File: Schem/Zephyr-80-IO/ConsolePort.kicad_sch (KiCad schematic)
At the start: 12 parts, among them J2 Conn_01x04, J3 0480370001, U2 FT230XS-U

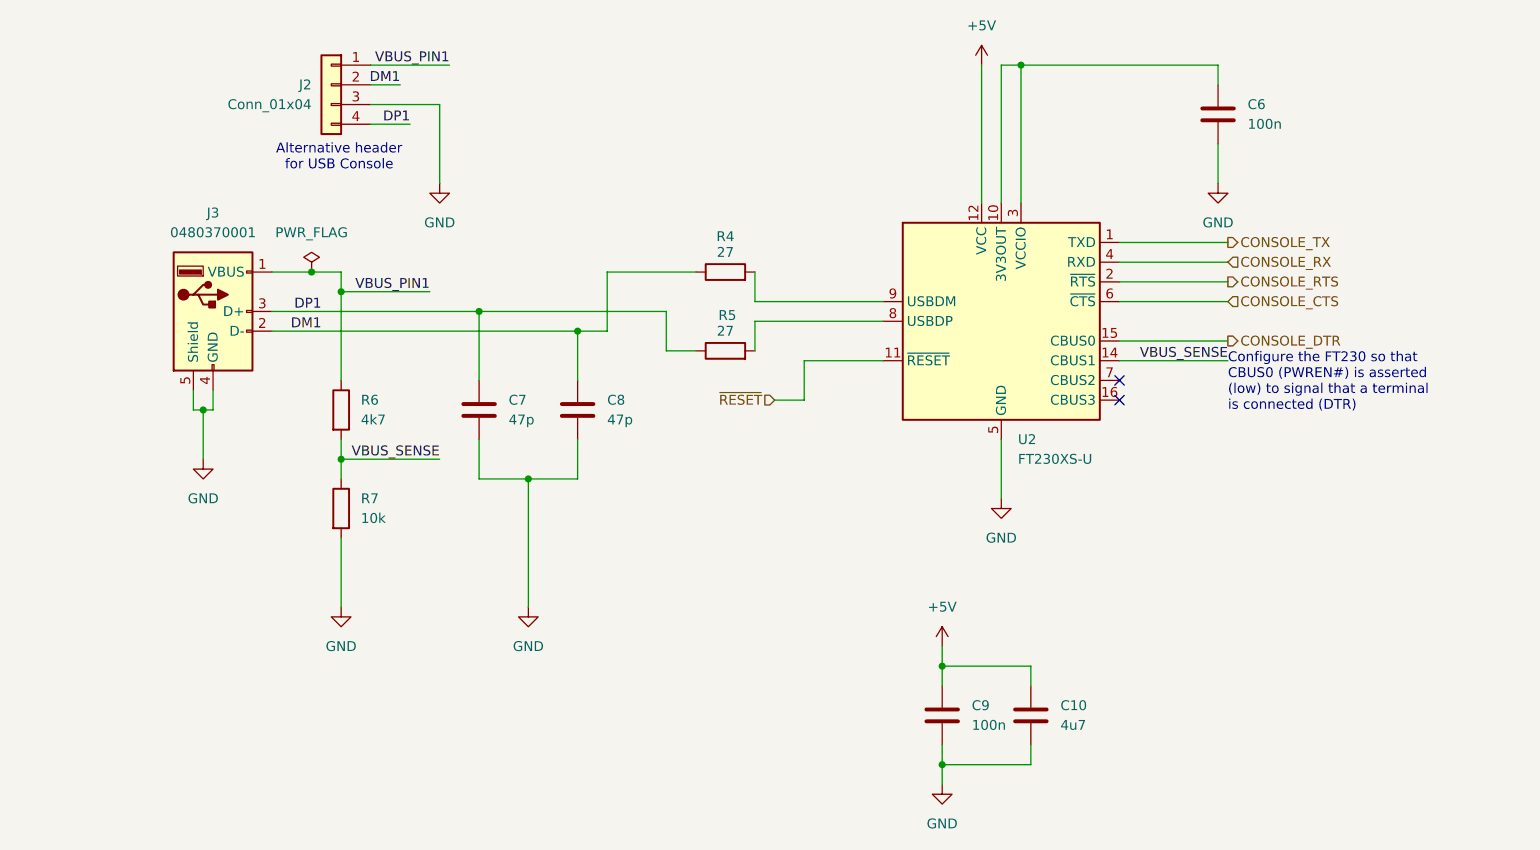
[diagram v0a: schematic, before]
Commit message: Completed the IO Controller schematic and PCB layout for the Zephyr-80 project. This includes the design of the Baud Clock, CPU Address Decoding, Console Port, Device Select Decode, GPIO User Serial, and the main IO Controller schematics. Additionally, the PCB layout for the Zephyr-80 IO board has been created, along with the necessary library files and documentation for the control signal mapping.
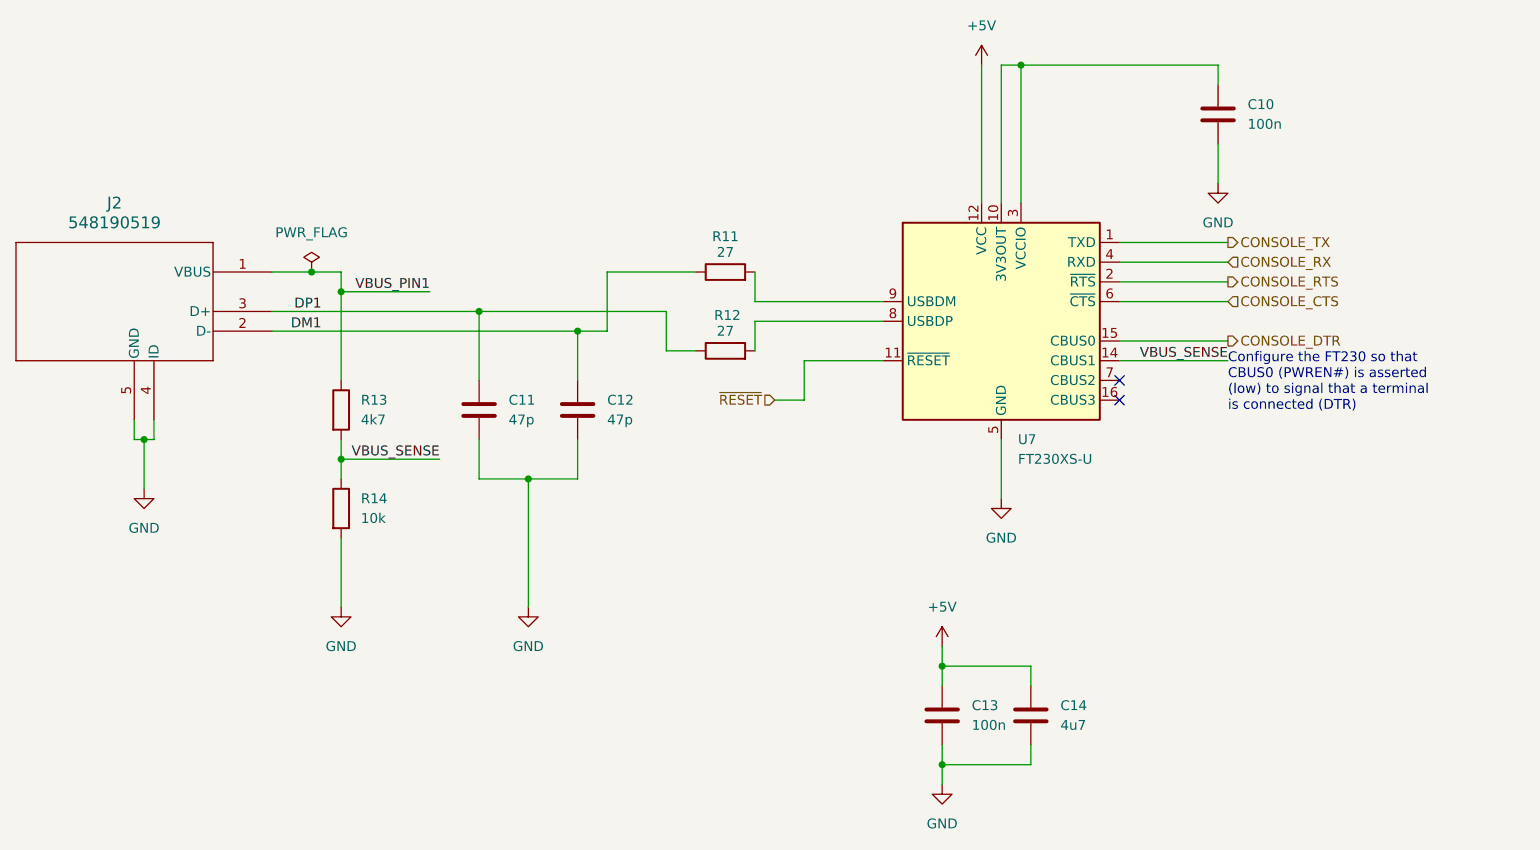
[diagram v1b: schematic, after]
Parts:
- removed J2: Conn_01x04, Connector_PinSocket_2.54mm:PinSocket_1x04_P2.54mm_Vertical, symbol Connector_Generic:Conn_01x04
- removed J3: 0480370001, Footprints:CONN_480370001_MOL, symbol Connector:USB_A
- added J2: 548190519, Footprints:54819-0519_MOL, symbol 2026-02-03_20-00-14:548190519
- renumbered C6 to C10, C7 to C11, C8 to C12, C9 to C13, C10 to C14, R4 to R11, R5 to R12, R6 to R13, R7 to R14, U2 to U7
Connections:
- net DM1: now also J2.2 (D-)
- net DP1: now also J2.3 (D+)
- net GND: now also J2.4 (ID), J2.5 (GND)
- net VBUS_PIN1: now also J2.1 (VBUS)
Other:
- note removed: "Alternative header for USB Console"

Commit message: Added all the manufacturer part numbers to the KiCad schematics and PCB files. This will make it easier to order the parts for the project and ensure that the correct components are used. I also removed some of the old schematics that were no longer needed, such as the BaudClock, ConsolePort, DeviceSelectDecode, GPIOUserSerial, IO Controller, UserPorts, Video, and Z80HomeBrew schematics. These changes will help to streamline the design and make it easier to understand.
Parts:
- J2: MANUFACTURER_PART_NUMBER (none) -> 0548190519
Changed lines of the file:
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@@
+			)
+		)
+		(property "MANUFACTURER_PART_NUMBER" "0548190519"
+			(at 21.59 62.23 0)
+			(effects
+				(font
+					(size 1.27 1.27)
+				)
+				(hide yes)
 			)
 		)

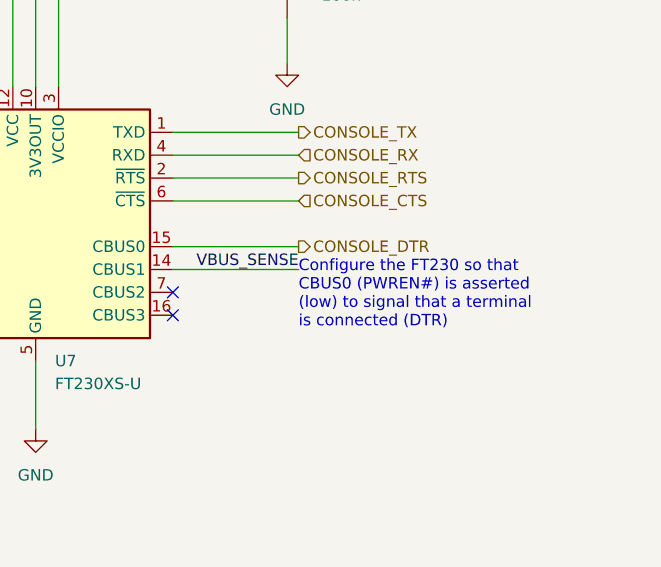
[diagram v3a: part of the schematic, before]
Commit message: Updated the IO Controller to properly support SDLC and SPI.
* Separated SPI1 and SPI2 and associated to the right pins.
      SPI1 is for devices (USB, SD Card and Controllers)
      SPI2 is for the SDLC controller (Z80 SIO1/A and B)

* Fixed the 1.27mm vs 2.54mm pin headers
* Fixed the power sequencing
* Fixed the pull ups
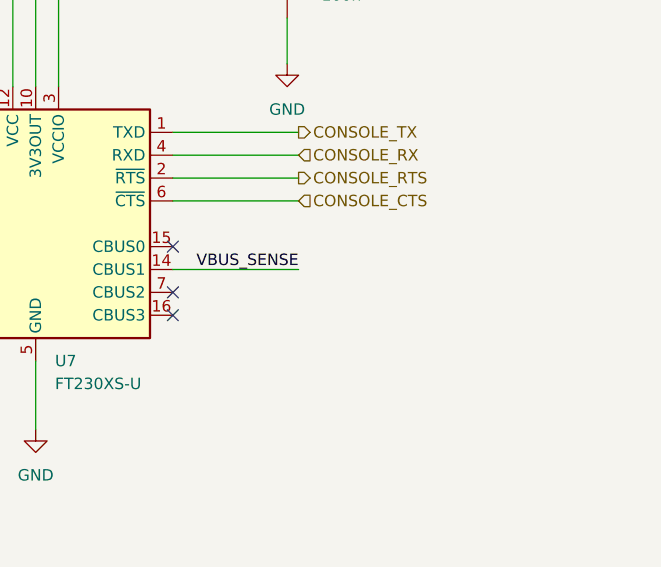
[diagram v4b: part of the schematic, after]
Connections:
- net CONSOLE_DTR: no longer names the net of U7.15 (CBUS0)
- no-connect marks 2 -> 3
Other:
- note removed: "Configure the FT230 so that CBUS0 (PWREN#) is asserted (low) to signal that a terminal is connected (DTR)"
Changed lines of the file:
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@@
 	(generator_version "10.0")
 	(paper "D")
-	(text "Configure the FT230 so that \nCBUS0 (PWREN#) is asserted \n(low) to signal that a terminal\nis connected (DTR)"
-		(exclude_from_sim no)
-		(at 185.42 75.184 0)
-		(effects
-			(font
-				(size 1.27 1.27)
-			)
-			(justify left)
-		)
-	)
 	(junction
 		(at 148.59 124.46)
@@
 		(at 171.45 74.93)
 	)
+	(no_connect
+		(at 171.45 69.85)
+	)
 	(wire
 		(pts
@@
 		(pts
 			(xy 45.72 82.55) (xy 44.45 82.55)
-		)
-		(stroke
-			(width 0)
-			(type default)
-		)
-	)
-	(wire
-		(pts
-			(xy 171.45 69.85) (xy 185.42 69.85)
 		)
 		(stroke
@@
 		(effects
 			(font
-				(size 1.27 1.27)
-			)
-			(justify left)
-		)
-	)
-	(hierarchical_label "CONSOLE_DTR"
-		(shape output)
-		(at 185.42 69.85 0)
-		(effects
-			(font
